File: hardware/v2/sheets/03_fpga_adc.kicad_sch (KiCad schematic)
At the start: 49 parts, among them U20 LIF-MD6000-6JMG80I, U21 AD9215BCPZ-105

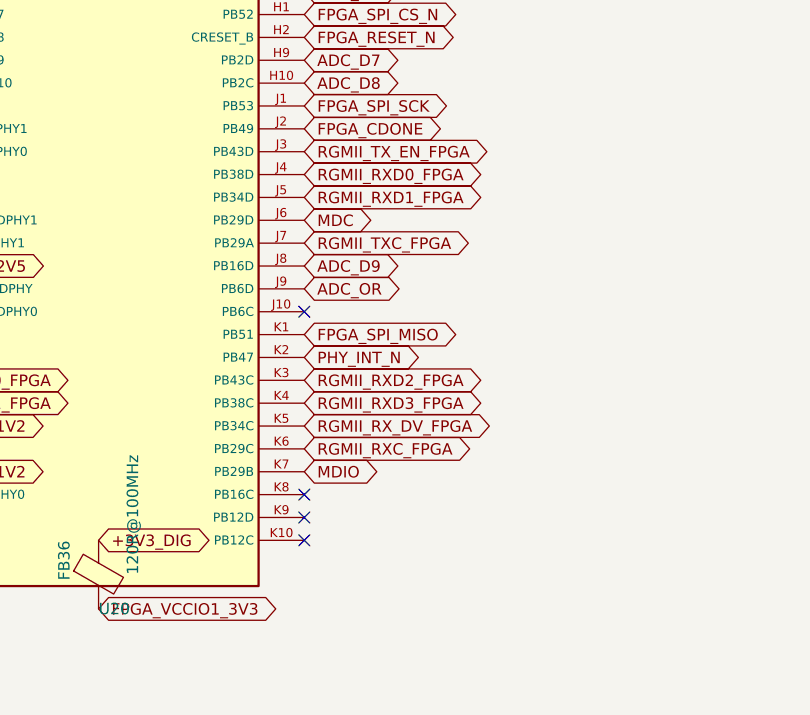
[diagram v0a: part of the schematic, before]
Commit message: Route timing-critical digital and analog nets
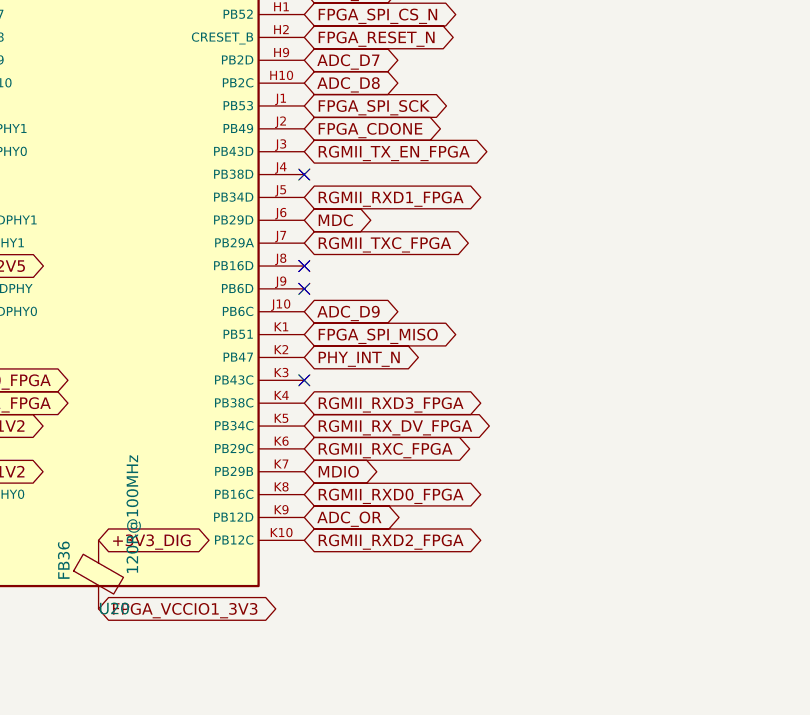
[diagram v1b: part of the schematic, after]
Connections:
- net ADC_D9: now also U20.J10 (PB6C); no longer U20.J8 (PB16D)
- net ADC_OR: now also U20.K9 (PB12D); no longer U20.J9 (PB6D)
- net RGMII_RXD0_FPGA: now also U20.K8 (PB16C); no longer U20.J4 (PB38D)
- net RGMII_RXD2_FPGA: now also U20.K10 (PB12C); no longer U20.K3 (PB43C)
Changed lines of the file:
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@@
 	)
 	(no_connect
-		(at 92.71 113.03)
-	)
-	(no_connect
-		(at 92.71 133.35)
-	)
-	(no_connect
-		(at 92.71 135.89)
-	)
-	(no_connect
-		(at 92.71 138.43)
+		(at 92.71 107.95)
+	)
+	(no_connect
+		(at 92.71 97.79)
+	)
+	(no_connect
+		(at 92.71 110.49)
+	)
+	(no_connect
+		(at 92.71 120.65)
 	)
 	(no_connect
@@
 	(global_label "RGMII_RXD0_FPGA"
 		(shape bidirectional)
-		(at 92.7100 97.7900 0)
-		(fields_autoplaced yes)
-		(effects
-			(font (size 1.27 1.27))
-			(justify left)
-		)
-		(property "Intersheetrefs" "${INTERSHEET_REFS}"
-			(at 95.2500 97.7900 0)
+		(at 92.7100 133.3500 0)
+		(fields_autoplaced yes)
+		(effects
+			(font (size 1.27 1.27))
+			(justify left)
+		)
+		(property "Intersheetrefs" "${INTERSHEET_REFS}"
+			(at 95.2500 133.3500 0)
 			(effects
 				(font (size 1.27 1.27))
@@
 	(global_label "ADC_D9"
 		(shape bidirectional)
-		(at 92.7100 107.9500 0)
-		(fields_autoplaced yes)
-		(effects
-			(font (size 1.27 1.27))
-			(justify left)
-		)
-		(property "Intersheetrefs" "${INTERSHEET_REFS}"
-			(at 95.2500 107.9500 0)
+		(at 92.7100 113.0300 0)
+		(fields_autoplaced yes)
+		(effects
+			(font (size 1.27 1.27))
+			(justify left)
+		)
+		(property "Intersheetrefs" "${INTERSHEET_REFS}"
+			(at 95.2500 113.0300 0)
 			(effects
 				(font (size 1.27 1.27))
@@
 	(global_label "ADC_OR"
 		(shape bidirectional)
-		(at 92.7100 110.4900 0)
-		(fields_autoplaced yes)
-		(effects
-			(font (size 1.27 1.27))
-			(justify left)
-		)
-		(property "Intersheetrefs" "${INTERSHEET_REFS}"
-			(at 95.2500 110.4900 0)
+		(at 92.7100 135.8900 0)
+		(fields_autoplaced yes)
+		(effects
+			(font (size 1.27 1.27))
+			(justify left)
+		)
+		(property "Intersheetrefs" "${INTERSHEET_REFS}"
+			(at 95.2500 135.8900 0)
 			(effects
 				(font (size 1.27 1.27))
@@
 	(global_label "RGMII_RXD2_FPGA"
 		(shape bidirectional)
-		(at 92.7100 120.6500 0)
-		(fields_autoplaced yes)
-		(effects
-			(font (size 1.27 1.27))
-			(justify left)
-		)
-		(property "Intersheetrefs" "${INTERSHEET_REFS}"
-			(at 95.2500 120.6500 0)
-			(effects
-				(font (size 1.27 1.27))
+		(at 92.7100 138.4300 0)
+		(fields_autoplaced yes)
+		(effects
+			(font (size 1.27 1.27))
+			(justify left)
+		)
+		(property "Intersheetrefs" "${INTERSHEET_REFS}"
+			(at 95.2500 138.4300 0)
+			(effects
+				(font (size 1.27 1.27))

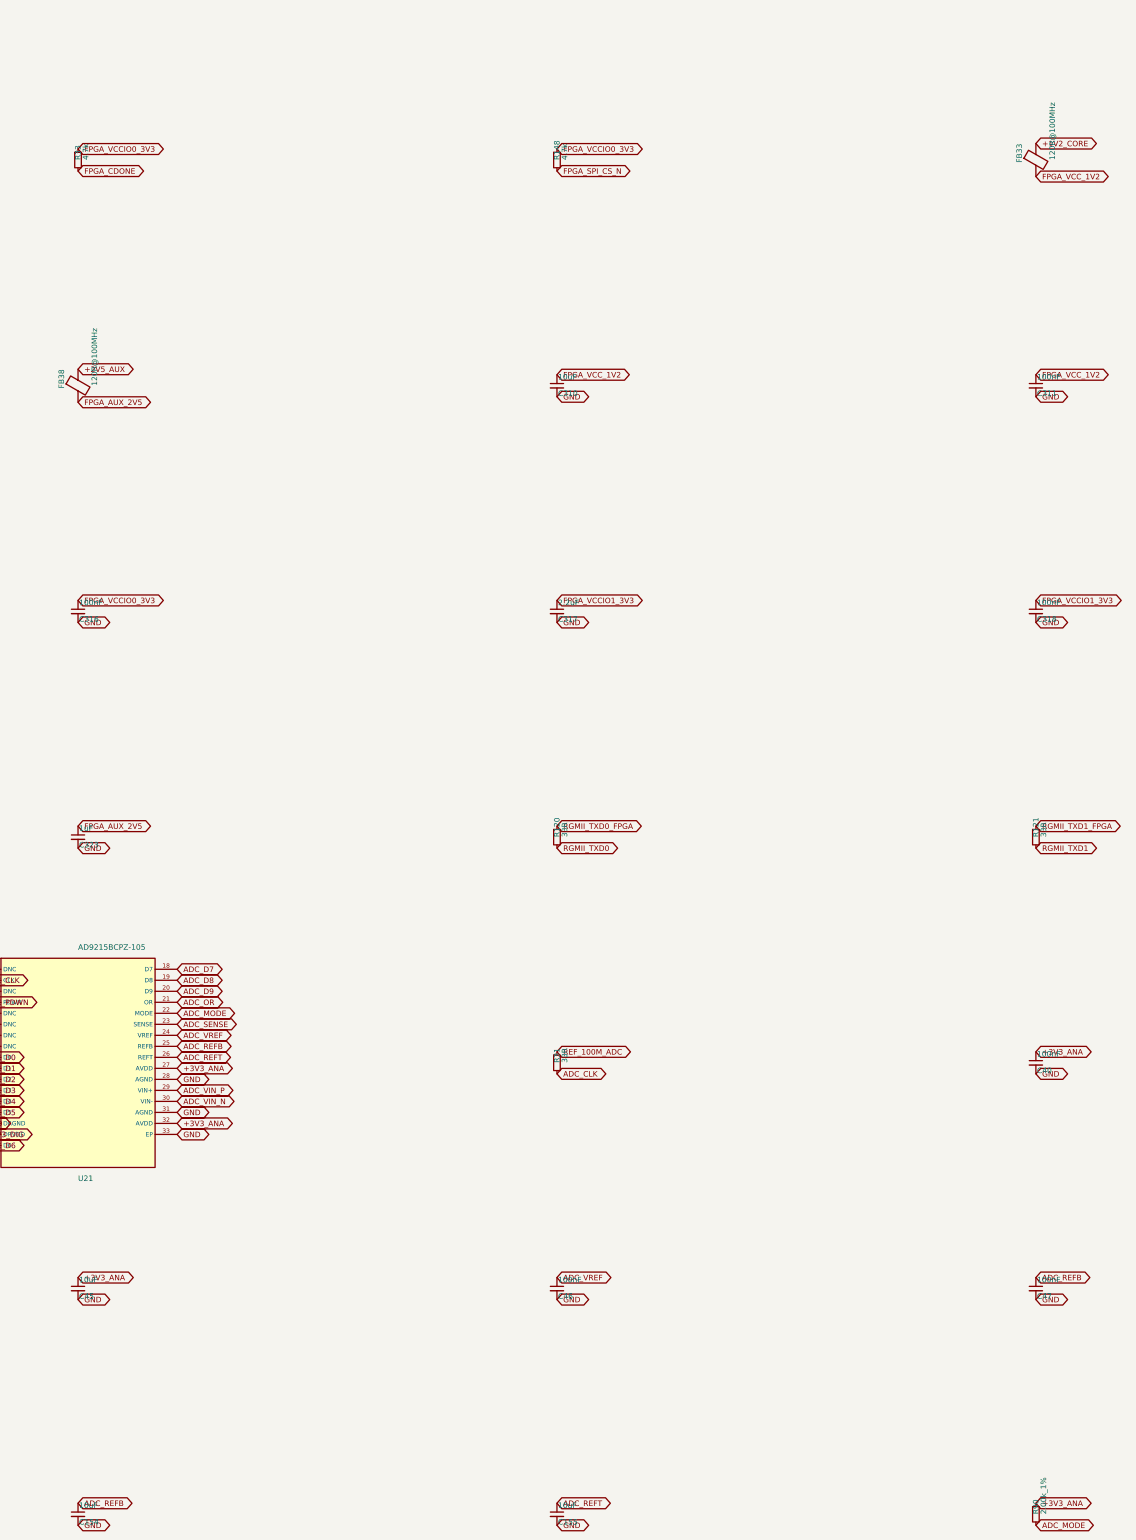
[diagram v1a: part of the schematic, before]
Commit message: hardware: checkpoint corrected V2 routing at 108 opens
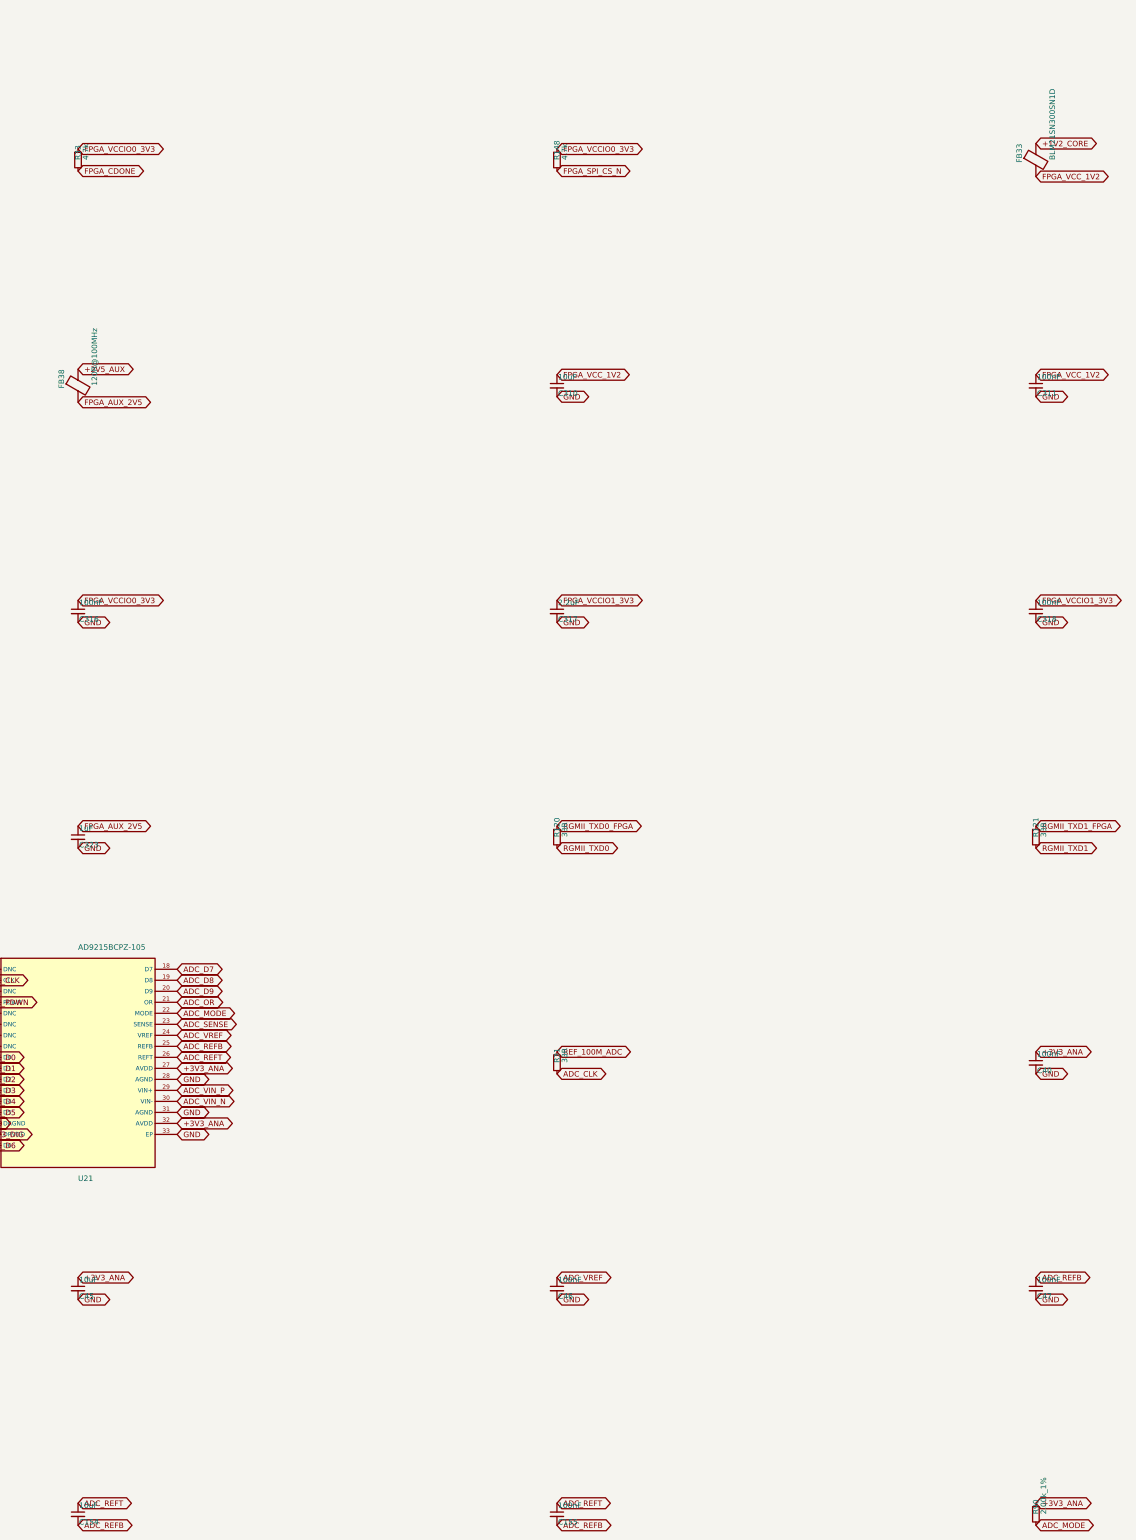
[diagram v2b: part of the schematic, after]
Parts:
- C155: value 10uF -> 100nF; footprint Capacitor_SMD:C_0805_2012Metric -> Capacitor_SMD:C_0402_1005Metric
- FB33: value 120R@100MHz -> BLM21SN300SN1D; footprint Inductor_SMD:L_0402_1005Metric -> Inductor_SMD:L_0805_2012Metric
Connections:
- net ADC_REFB: now also C154.2, C155.2; no longer C154.1
- net ADC_REFT: now also C154.1
- net GND: no longer C154.2, C155.2
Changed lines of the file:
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@@
 			)
 		)
-		(property "Value" "120R@100MHz"
+		(property "Value" "BLM21SN300SN1D"
 			(at 514.35 90.17 90)
 			(effects
@@
 			)
 		)
-		(property "Footprint" "Inductor_SMD:L_0402_1005Metric"
+		(property "Footprint" "Inductor_SMD:L_0805_2012Metric"
 			(at 508.762 90.17 90)
 			(effects
@@
 			)
 		)
-		(property "Description" ""
+		(property "Description" "Murata 30R@100MHz, 5mOhm maximum DCR after test; 0.5A core allocation, total distribution drop at most 10mV"
 			(at 510.54 90.17 0)
 			(effects
@@
 			)
 		)
-		(property "Description" "ADC_REFB local bypass"
+		(property "Description" "AD9215 Figure 36 direct REFT-to-REFB bulk reference capacitor"
 			(at 289.56 402.59 0)
 			(effects
@@
 			)
 		)
-		(property "Value" "10uF"
+		(property "Value" "100nF"
 			(at 400.304 400.558 0.0000)
 			(effects
@@
 			)
 		)
-		(property "Footprint" "Capacitor_SMD:C_0805_2012Metric"
+		(property "Footprint" "Capacitor_SMD:C_0402_1005Metric"
 			(at 400.05 402.59 0.0000)
 			(effects
@@
 			)
 		)
-		(property "Description" "ADC_REFT local bypass"
+		(property "Description" "AD9215 Figure 36 direct reference bypass; place at pins 25 and 26"
 			(at 400.05 402.59 0)
 			(effects
@@
 		)
 	)
-	(global_label "ADC_REFB"
+	(global_label "ADC_REFT"
 		(shape bidirectional)
 		(at 289.5600 400.0500 0)
@@
 		)
 	)
-	(global_label "GND"
+	(global_label "ADC_REFB"
 		(shape bidirectional)
 		(at 289.5600 405.1300 0)
@@
 		)
 	)
-	(global_label "GND"
+	(global_label "ADC_REFB"
 		(shape bidirectional)
 		(at 400.0500 405.1300 0)
